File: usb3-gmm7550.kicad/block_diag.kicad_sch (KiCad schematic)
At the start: 0 parts

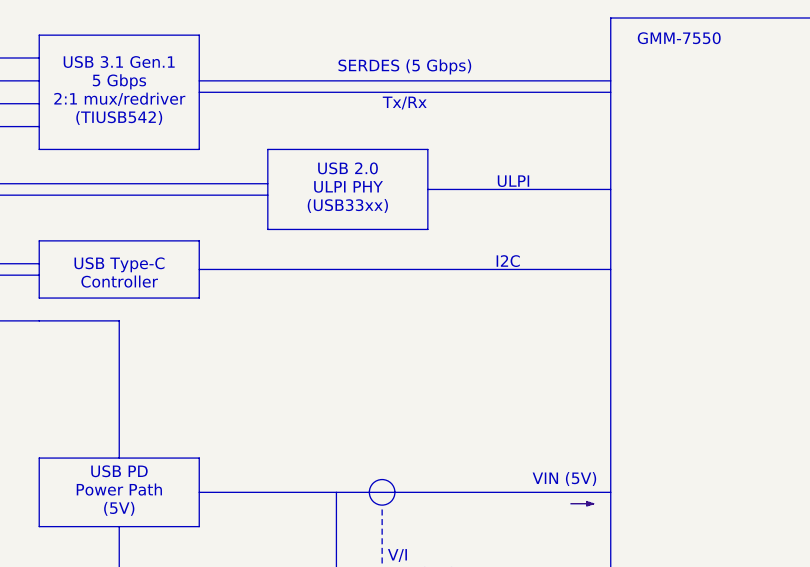
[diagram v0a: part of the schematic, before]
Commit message: Add USB 1.1 Driver/Receiver implementation option
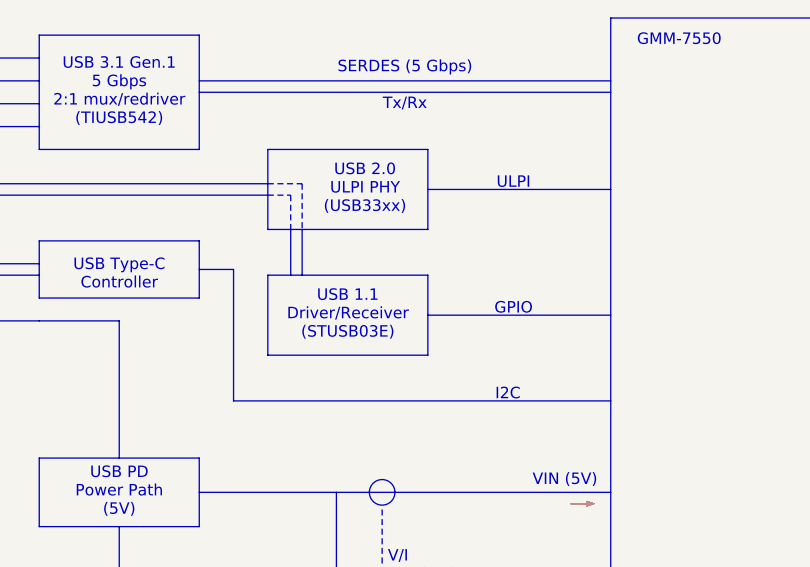
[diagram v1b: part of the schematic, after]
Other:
- note added: "GPIO"
- note added: "USB 1.1 Driver/Receiver (STUSB03E)"
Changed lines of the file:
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@@
 	)
 	(rectangle
+		(start 127 60.325)
+		(end 144.78 69.215)
+		(stroke
+			(width 0)
+			(type default)
+		)
+		(fill
+			(type none)
+		)
+	)
+	(rectangle
 		(start 127 110.49)
 		(end 144.78 128.27)
@@
 	(text "USB 2.0\nULPI PHY\n(USB33xx)"
 		(exclude_from_sim no)
-		(at 135.89 50.8 0)
+		(at 137.795 50.8 0)
 		(effects
 			(font
@@
 		)
 	)
+	(text "USB 1.1\nDriver/Receiver\n(STUSB03E)"
+		(exclude_from_sim no)
+		(at 135.89 64.77 0)
+		(effects
+			(font
+				(size 1.27 1.27)
+			)
+		)
+	)
 	(text "VBUS"
 		(exclude_from_sim no)
@@
 	(text "I2C"
 		(exclude_from_sim no)
-		(at 153.67 59.055 0)
+		(at 153.67 73.66 0)
 		(effects
 			(font
@@
 		)
 	)
+	(text "GPIO"
+		(exclude_from_sim no)
+		(at 154.305 64.135 0)
+		(effects
+			(font
+				(size 1.27 1.27)
+			)
+		)
+	)
 	(text "RP2040"
 		(exclude_from_sim no)
@@
 	(polyline
 		(pts
+			(xy 130.81 50.165) (xy 130.81 55.245)
+		)
+		(stroke
+			(width 0)
+			(type dot)
+		)
+	)
+	(polyline
+		(pts
 			(xy 101.6 65.405) (xy 110.49 65.405)
 		)
@@
 	(polyline
 		(pts
+			(xy 119.38 59.69) (xy 123.19 59.69)
+		)
+		(stroke
+			(width 0)
+			(type default)
+		)
+	)
+	(polyline
+		(pts
 			(xy 81.28 41.275) (xy 101.6 41.275)
 		)
@@
 	(polyline
 		(pts
+			(xy 123.19 74.295) (xy 123.19 59.69)
+		)
+		(stroke
+			(width 0)
+			(type default)
+		)
+	)
+	(polyline
+		(pts
 			(xy 81.28 34.925) (xy 81.28 66.675)
 		)
@@
 	(polyline
 		(pts
+			(xy 144.78 64.77) (xy 165.1 64.77)
+		)
+		(stroke
+			(width 0)
+			(type default)
+		)
+	)
+	(polyline
+		(pts
 			(xy 81.28 101.6) (xy 81.28 133.35)
 		)
@@
 	(polyline
 		(pts
+			(xy 130.81 55.245) (xy 130.81 60.325)
+		)
+		(stroke
+			(width 0)
+			(type default)
+		)
+	)
+	(polyline
+		(pts
 			(xy 76.2 34.925) (xy 76.2 66.675)
 		)
@@
 	(polyline
 		(pts
+			(xy 129.54 55.245) (xy 129.54 60.325)
+		)
+		(stroke
+			(width 0)
+			(type default)
+		)
+	)
+	(polyline
+		(pts
 			(xy 83.82 51.435) (xy 81.28 51.435)
 		)
@@
 	(polyline
 		(pts
-			(xy 119.38 59.69) (xy 165.1 59.69)
+			(xy 123.19 74.295) (xy 165.1 74.295)
 		)
 		(stroke
@@
 		)
 	)
+	(polyline
+		(pts
+			(xy 127 50.165) (xy 130.81 50.165)
+		)
+		(stroke
+			(width 0)
+			(type dot)
+		)
+	)
+	(polyline
+		(pts
+			(xy 129.54 51.435) (xy 129.54 55.245)
+		)
+		(stroke
+			(width 0)
+			(type dot)
+		)
+	)
+	(polyline
+		(pts
+			(xy 127 51.435) (xy 129.54 51.435)
+		)
+		(stroke
+			(width 0)
+			(type dot)
+		)
+	)
 	(image
 		(at 191.135 84.455)
@@
 			"ACwAAK+4BAAALgAAACwAAAAuAACvuAQAACwAAK+4BAAALgAAr7kEAAAsAACvuQQAAC4AAAAsAAAA"
 			"LgAAr7UEAAAsAACvtQQAAC4AAK+2BAAALAAAr7YEAAAuAAAALAAAAC4AAK6wBAAALAAArrAEAAAu"
-			"AACusgQAACw="
+			"AACusgQAACwAAAAAAAAAAAAAAAAAAAAAAAAAAAAAAAAAAAAAAAAAAAAAAAAAAAAAAAAAAAAAAAAA"
+			"AAAAAAAAAAAAAAAAAAAAAAAAAAAAAAAAAAAAAAAAAAAAAAAAAAAAAAAAAAAAAAAAAAAAAAAAAAAA"
+			"AAAAAAAAAAAAAAAAAAAAAAAAAAAAAAAAAAAAAAAAAAAAAAAAAAAAAAAAAAAAAAAAAAAAAAAAAAAA"
+			"AAAAAAAAAAAAAAAAAAAAAAAAAAAAAAAAAAAAAAAAAAAAAAAAAAAAAAAAAAAAAAAAAAAAAAAAAAAA"
+			"AAAAAAAAAAAAAAAAAAAAAAAAAAAAAAAAAAAAAAAAAAAAAAAAAAAAAAAAAAAAAAAAAAAAAAAAAAAA"
+			"AAAAAAAAAAAAAAAAAAAAAAAAAAAAAAAAAAAAAAAAAAAAAAAAAAAAAAAAAAAAAAAAAAAAAAAAAAAA"
+			"AAAAAAAAAAAAAAAAAAAAAAAAAAAAAAAAAAAAAAAAAAAAAAAAAAAAAAAAAAAAAAAAAAAAAAAAAAAA"
+			"AAAAAAAAAAAAAAAAAAAAAAAAAAAAAAAAAAAAAAAAAAAAAAAAAAAAAAAAAAAAAAAAAAAAAAAAAAAA"
+			"AAAAAAAAAAAAAAAAAAAAAAAAAAAAAAAAAAAAAAAAAAAAAAAAAAAAAAAAAAAAAAAAAAAAAAAAAAAA"
+			"AAAAAAAAAAAAAAAAAAAAAAAAAAAAAAAAAAAAAAAAAAAAAAAAAAAAAAAAAAAAAAAAAAAAAAAAAAAA"
+			"AAAAAAAAAAAAAAAAAAAAAAAAAAAAAAAAAAAAAAAAAAAAAAAAAAAAAAAAAAAAAAAAAAAAAAAAAAAA"
+			"AAAAAAAAAAAAAAAAAAAAAAAAAAAAAAAAAAAAAAAAAAAAAAAAAAAAAAAAAAAAAAAAAAAAAAAAAAAA"
+			"AAAAAAAAAAAAAAAAAAAAAAAAAAAAAAAAAAAAAAAAAAAAAAAAAAAAAAAAAAAAAAAAAAAAAAAAAAAA"
+			"AAAAAAAAAAAAAAAAAAAAAAAAAAAAAAAAAAAAAAAAAAAAAAAAAAAAAAAAAAAAAAAAAAAAAAAAAAAA"
+			"AAAAAAAAAAAAAAAAAAAAAAAAAAAAAAAAAAAAAAAAAAAAAAAAAAAAAAAAAAAAAAAAAAAAAAAAAAAA"
+			"AAAAAAAAAAAAAAAAAAAAAAAAAAAAAAAAAAAAAAAAAAAAAAAAAAAAAAAAAAAAAAAAAAAAAAAAAAAA"
+			"AAAAAAAAAAAAAAAAAAAAAAAAAAAAAAAAAAAAAAAAAAAAAAAAAAAAAAAAAAAAAAAAAAAAAAAAAAAA"
+			"AAAAAAAAAAAAAAAAAAAAAAAAAAAAAAAAAAAAAAAAAAAAAAAAAAAAAAAAAAAAAAAAAAAAAAAAAAAA"
+			"AAAAAAAAAA=="
 		)
 	)
@@
 			"AAAAAAAAAAAAAAAAAAAAAAAAAAAAAAAAAAAAAAAAAAAAAAAAAAAAAAAAAAAAAAAAAAAAAAAAAAAA"
 			"AAAAAAAAAAAAAAAAAAAAAAAAAAAAAAAAAAAAAAAAAAAAAAAAAAAAAAAAAAAAAAAAAAAAAAAAAAAA"
-			"AAAAAAAAAAAAAAAAAA=="
+			"AAAAAAAAAAAAAAAAAAAAAAAAAAAAAAAAAAAAAAAAAAAAAAAAAAAAAAAAAAAAAAAAAAAAAAAAAAAA"
+			"AAAAAAAAeHNxczU3dU5pMGhCRldCWDc0cGFnUWRPkSoAAAAAAAAQ8u/7SHgAABDx89hnXQAAEPHz"
+			"2GddAAAQ8fPYZ10AADVBQmVyejFqWVNaODZqRTA3RSsyTElNNkg1TzJ6YmxFS21QT0IxeDRqcG91"
+			"eTJDZHNiL3E0TkFBbDMwSGVtRGZ5M2xKSlNsMTlYakVteGRpMjRFSU9WK3RmQTFQd2lBdVZqb1RX"
+			"ME1QUUtpcWVjNFFUdWRiTkM2RXNMSU5nRW95dHl5bDJwbUY0QkpCaUtFVUdoSEdIUzZVMlVPOXVw"
+			"a3NFVVNYWG9wVjQ2ZG1lbjlHWHAvUmxSZTN1LzJQL25QSXdHYTZsUWhFM3JubkthMUtBRHlHbG5u"
+			"SDBJWWg3Q1puQ3l2SHdXTTBPdnJUOVpzUFAyWnZHZHJZQjFBazhQUFB5UEhrK25TU0JvWVdJbzBZ"
+			"VXlJamF2QzBBMEwxZmpnWmZhQ3lTNlRYMXhUNFFVK0EwYVFNSjdsL0dUcEdrM0NWT05oeWdoT2NL"
+			"MDZLVDlCa2VlcDNnWTErYjFFQnBkYVhpRUlBc0dwS1lDY3NMMWNRY2V5Y1o1QURXM1hKUmRaekx6"
+			"TmJMNEVwdkQyQ2FnRUY1SjVUSG5UMGc2Z3F6WTJtS2U4WnhMMmZzby9iSURkR0dDMld1bnU4NVF4"
+			"QXNCdWxyZ3ZidzRESlFZeDFLa0F1M2pCdDlCZXlBMWlMME9JT05GSld0SWhleUpweHFRcndJRkRm"
+			"bGxuZXNCdnpOVXYxd2ltMjBRZ2QyNDFwZU1rVUhlenUzS29ZQ21sRlE2MDV0VUZtSEpOZWNheWs5"
+			"U3FUeGdEUk0wbXlKS1VxQzJBdTloY25jVXA0VmRnVFM4S1BNYjRHSlZJckJKVFNEbFVocE1RVUJ0"
+			"ZUpJQU5NVW1UdjRGcEFJMG9tdWJZOFZGRkRlNFBjeWt3UWFOSVlZcEhrQTFBZlpSRW5ZcUtqVTVP"
+			"TzJBRTBQTjBQL1BoUXkwNnBUZTJReVA4QWovckRLbStabUVTdWtPTWJ3cTdvbVZSWjV5NnVzSFNI"
+			"b3RjcUVjT01JRFErcWdiMiswd3JvZlZ3QTFhRWEwRy9Zam1lazBKMG9DSzdLRzVwN0hsTkNVcHVK"
+			"MjYzaHNKQlJOVGdUT2RpZU1aZGNnQkRTZGhvd2h3U2trS0ZDUUhEdnc0VE1JRHdmRXA5SndSTWVh"
+			"Vjkrbi8yOU9ma1pLSmVFdENzRGVDR3lGUUNWRFF4bkx2TldWeTZLMUZBdXUzMXMxdW1GRFVETnFj"
+			"L2JPQUZvZFlKS1VmRQ=="
 		)
 	)
@@
 			"AAAAAAAAAAAAAAAAAAAAAAAAAAAAAAAAAAAAAAAAAAAAAAAAAAAAAAAAAAAAAAAAAAAAAAAAAAAA"
 			"AAAAAAAAAAAAAAAAAAAAAAAAAAAAAAAAAAAAAAAAAAAAAAAAAAAAAAAAAAAAAAAAAAAAAAAAAAAA"
-			"AAAAAAAAAAAAAAAAAAAAAA=="
+			"AAAAAAAAAAAAAAAAAAAAAAAKAAAA/v8AAAAAAAAAAP///v/+/wAAAQAAAP////8BAAAAAAAAAAAA"
+			"AAAAAAAA+v4CAAcA/f///wAAAgAEAPn/AwADAP///v8AAAEA/v//////BAD+////AQAAAAAAAQD+"
+			"/wMA/f8BAAAAAAAAAAAAAAAAAP//AQD//wAAAAD//wEA//8AAAAAAAAAAAAAAAAAAAAAAAAAAAAA"
+			"AAAAAAAAAAAAAAAAAAAAAAAAAADg/gkABAD9/wEAAAAAAAAACQAMAPv//////wEAAAAAAAEA/P/6"
+			"//3/AQAAAAAAAAD///z//f8AAAEAAQAAAAAAAAABAAAAAQABAAAAAAAAAAEAAAAAAAEAAQAAAAAA"
+			"AAAAAAAAAAAAAAAAAAAAAAAAAAAAAAAAAAAAAAAAAAAAAPD+BQD6/wEAAQABAAEAAAD//+7//f//"
+			"/////////wAA+/8CAP3///8CAAAAAQAAAP7/AQD9/wcAAgD//wAAAAAAAAEAAQACAP3///8AAAAA"
+			"AAAAAAAA/////wEAAAAAAAAAAAAAAAAAAAAAAAAAAAAAAAAAAAAAAAAAAAAAAAAA2f4HAAUAAgAA"
+			"AAAAAAAAAAcACQAEAAIAAAAAAAAAAAADAAQAAwABAAAAAAAAAAAAAgACAAEAAAAAAAAAAAAAAAAA"
+			"AAAAAAAAAAAAAAAAAAAAAAAAAAAAAAAAAAAAAAAAAAAAAAAAAAAAAAAAAAAAAAAAAAAAAAAAAAAA"
+			"AAAAAADi/g8A+v/1//z/AAABAAAA5v/r/wYACwAGAAAA/////w8ADAD7//j//f8AAAEAAAD0//b/"
+			"AwAFAAIAAAAAAAAABwAGAP///v///wAAAAAAAPz//v8AAAEAAQAAAAAAAAABAAEAAAD//wAAAAAA"
+			"AAAAAAAAAAAAAAAAAAAAAAAAAGL/R/8IAA4AEgDy/wMAAQCFAJ//5f8bAAMA/P///wMA5v8XAPz/"
+			"AgD9/wEAAAAAANX/HwAGAP7//f8AAAMA/v8DAPj/BAABAAAA/v8DAP7///8DAPz/BAD+/wAAAAAA"
+			"AP3/AgABAP//AAAAAP//AAD9/wIAAQD//wAAAQAAAAAAuv8cAAYA/P8QAAEA/v////4A5f/u/+7/"
+			"BAD///3/AQDx/wQAFQAEAAEAAwD9/wMArf/x/wUAAwACAAQA//8BAAIADAAJAAYABgAEAAAA//8I"
+			"AP////8AAAEAAQD//////P8AAAAA//8AAAAAAAAAAPr///////////8BAAAA//9v/6z/3P/r/wIA"
+			"BgAGAAkAvwDA/+f/7/8EAAQABAAGAO3/DwD1//n/AgACAP///P/M/xkA/P/8////AgD9//3//P8D"
+			"AP7//v/+/wEA//8AAAcA/w=="
 		)
 	)
